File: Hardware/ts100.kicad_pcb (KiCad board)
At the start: 2 copper layers, 100 x 17 mm, 0 parts

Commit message: pcb
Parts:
- added C1: 0.1u, Capacitor_SMD:C_0603_1608Metric, F.Cu at (154.0, 137.6)
- added C10: 0.1u, Capacitor_SMD:C_0603_1608Metric, F.Cu at (148.9, 140.1)
- added C11: 0.1u, Capacitor_SMD:C_0603_1608Metric, F.Cu at (148.9, 142.6)
- added C12: 0.1u, Capacitor_SMD:C_0603_1608Metric, F.Cu at (153.0, 140.1)
- added C13: 0.1u, Capacitor_SMD:C_0603_1608Metric, F.Cu at (166.4, 128.7)
- added C2: 10u, Capacitor_SMD:C_0805_2012Metric, F.Cu at (161.1, 130.0)
- added C3: 0.1u, Capacitor_SMD:C_0603_1608Metric, F.Cu at (165.0, 140.0)
- added C4: 2.2n, Capacitor_SMD:C_0603_1608Metric, F.Cu at (173.3, 131.6)
- added C5: 10n, Capacitor_SMD:C_0603_1608Metric, F.Cu at (169.3, 131.2)
- added C6: 22u, Capacitor_SMD:C_0805_2012Metric, F.Cu at (156.2, 132.2)
- added C7: 22p, Capacitor_SMD:C_0603_1608Metric, F.Cu at (160.0, 135.0)
- added C8: 22p, Capacitor_SMD:C_0603_1608Metric, F.Cu at (156.0, 135.0)
- added C9: 0.1u, Capacitor_SMD:C_0603_1608Metric, F.Cu at (150.0, 137.6)
- added D1: 1N5819, Diode_SMD:D_SMA, F.Cu at (142.9, 140.4)
- added J2: Iron+, ts100:Fuseholder_5x20mm_inline, F.Cu at (137.2, 119.6)
- added J3: Iron-, ts100:Fuseholder_5x20mm_inline, F.Cu at (141.9, 103.8)
- added J4: GND, ts100:Fuseholder_5x20mm_inline, F.Cu at (99.3, 102.9)
- added J5: SWD, Connector_PinHeader_1.27mm:PinHeader_2x03_P1.27mm_Vertical, F.Cu at (161.0, 124.3)
- added L1: 6.8u, ts100:Inductor_SMD_5x4.5mm, F.Cu at (149.4, 133.5)
- added Q1: 2SC3356, Package_TO_SOT_SMD:SOT-23, F.Cu at (166.6, 125.1)
- added Q2: IRF4905STRLPBF, Package_TO_SOT_SMD:TO-263-2, B.Cu at (125.0, 101.1)
- added R1: 1k, Resistor_SMD:R_0603_1608Metric, F.Cu at (168.0, 133.7)
- added R10: 10k, Resistor_SMD:R_0603_1608Metric, F.Cu at (170.8, 124.1)
- added R11: 31.25k, Resistor_SMD:R_0603_1608Metric, F.Cu at (161.0, 140.0)
- added R12: 1M, Resistor_SMD:R_0603_1608Metric, F.Cu at (173.3, 129.1)
- added R13: 10k, Resistor_SMD:R_0603_1608Metric, F.Cu at (161.0, 142.5)
- added R14: 10k, Resistor_SMD:R_0603_1608Metric, F.Cu at (166.0, 136.2)
- added R2: 1k, Resistor_SMD:R_0603_1608Metric, F.Cu at (153.0, 142.6)
- added R3: 100k, Resistor_SMD:R_0603_1608Metric, F.Cu at (158.0, 137.5)
- added R4: 1k, Resistor_SMD:R_0603_1608Metric, F.Cu at (165.3, 131.2)
- added R5: 10k, Resistor_SMD:R_0603_1608Metric, F.Cu at (170.8, 126.6)
- added R6: 10k, Resistor_SMD:R_0603_1608Metric, F.Cu at (157.0, 140.1)
- added R7: 51k, Resistor_SMD:R_0603_1608Metric, F.Cu at (164.0, 133.7)
- added R8: 10k, Resistor_SMD:R_0603_1608Metric, F.Cu at (157.0, 142.6)
- added R9: 1k, Resistor_SMD:R_0603_1608Metric, F.Cu at (162.0, 137.5)
- added RV1: 500k, ts100:3362P, F.Cu at (170.2, 118.7)
- added U1: AD823, Package_SO:SOP-8_3.9x4.9mm_P1.27mm, F.Cu at (134.7, 141.4)
- added U2: EUP3476, Package_SO:SOIC-8-1EP_3.9x4.9mm_P1.27mm_EP2.29x3mm_ThermalVias, F.Cu at (126.2, 140.5)
- added U3: 1N4728A, Diode_THT:D_DO-41_SOD81_P7.62mm_Horizontal, F.Cu at (123.9, 135.2)
- added U4: 128x32 OLED, Connector_PinSocket_2.54mm:PinSocket_1x04_P2.54mm_Vertical, F.Cu at (156.5, 97.5)
- added U5: STM32F103C8T6, Package_QFP:LQFP-48_7x7mm_P0.5mm, F.Cu at (142.3, 132.5)
- added Y1: 8M, Crystal:Crystal_SMD_HC49-SD, F.Cu at (129.3, 129.9)

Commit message: pcb
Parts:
- added J1: Jack-DC, KIGIT_Connector:DC-050_2.5x5.5mm_SMT, F.Cu at (193.9, 106.4)
- added S1: SW18010P, Capacitor_THT:C_Radial_D5.0mm_H5.0mm_P2.00mm, B.Cu at (115.0, 100.0)
- added SW1: SW_Push, ts100:SMD,4.6x1.82x3.5mm, F.Cu at (115.5, 94.1)
- added SW2: SW_Push, ts100:SMD,4.6x1.82x3.5mm, F.Cu at (115.5, 108.0)
- C1, C10, C11, C12, C13, C7, C8, C9, D1, R10, R12, R13, R14, R4, R7, R9, RV1, U1, U3, U5, Y1: moved to B.Cu
- J5: footprint Connector_PinHeader_1.27mm:PinHeader_2x03_P1.27mm_Vertical -> Connector_PinHeader_1.27mm:PinHeader_1x06_P1.27mm_Vertical
- Q2: moved to F.Cu
- moved D1 75.9 mm to (142.5, 64.5)
- moved RV1 75.7 mm to (112.8, 69.3)
- moved C1 75.3 mm to (135.1, 64.7)
- moved R9 74.7 mm to (159.7, 62.9)
- moved R7 74.5 mm to (151.9, 60.1)
- moved U3 74.3 mm to (157.3, 68.8)
- moved U1 72.5 mm to (103.8, 75.8)
- moved U2 69.2 mm to (194.6, 151.2)
- moved R4 67.9 mm to (151.0, 64.8)
- moved R10 67.2 mm to (158.2, 58.1)
- moved J5 65.2 mm to (103.2, 94.2), turned to 270 degrees
- moved Q1 63.5 mm to (106.5, 145.5)
- moved R5 60.9 mm to (111.6, 140.8)
- moved C6 57.6 mm to (210.7, 151.0)
- moved R2 55.5 mm to (204.2, 163.9)
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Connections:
- J5 pad 1: +3V3 -> GND
- J5 pad 2: GND -> +3V3
- J5 pad 4: /SWDCLK -> /SWO
- J5 pad 5: /SWO -> /SWDCLK
- U5 pad 21: Net-(U5-Pad21) -> /WAK_UP
- U5 pad 45: Net-(U5-Pad45) -> /KEY1
- U5 pad 46: Net-(U5-Pad46) -> /KEY2

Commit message: 修改封装
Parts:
- removed R14: 10k, Resistor_SMD:R_0603_1608Metric
- removed SW1, SW2: SW_Push, ts100:SMD,4.6x1.82x3.5mm
- added C14: 0.1u, Capacitor_SMD:C_0402_1005Metric, F.Cu at (191.0, 80.0)
- added D2: 1N5819, Diode_SMD:D_SOD-123, F.Cu at (182.8, 75.3)
- added FB1: 600@100MHz, Inductor_SMD:L_0805_2012Metric, F.Cu at (187.3, 78.9)
- added K1: TMP_UP, ts100:SMD,4.6x1.82x3.5mm, F.Cu at (181.9, 79.3)
- added K2: TMP_DOWN, ts100:SMD,4.6x1.82x3.5mm, F.Cu at (189.9, 74.7)
- added L2: 39n, Inductor_SMD:L_0402_1005Metric, F.Cu at (191.0, 78.0)
- C1: value 0.1u -> 10u 50V; footprint Capacitor_SMD:C_0603_1608Metric -> Capacitor_SMD:C_1210_3225Metric
- C10: value 0.1u -> 1u; footprint Capacitor_SMD:C_0603_1608Metric -> Capacitor_SMD:C_0402_1005Metric
- C11: value 0.1u -> 10n; footprint Capacitor_SMD:C_0603_1608Metric -> Capacitor_SMD:C_0402_1005Metric
- C12, C13: value 0.1u -> 12p; footprint Capacitor_SMD:C_0603_1608Metric -> Capacitor_SMD:C_0402_1005Metric
- C2: value 10u -> 10n; footprint Capacitor_SMD:C_0805_2012Metric -> Capacitor_SMD:C_0603_1608Metric
- C3: value 0.1u -> 22u 6.3V
- C4: value 2.2n -> 0.1u
- C5: value 10n -> 4u7; footprint Capacitor_SMD:C_0603_1608Metric -> Capacitor_SMD:C_0402_1005Metric
- C6: value 22u -> 0.1u; footprint Capacitor_SMD:C_0805_2012Metric -> Capacitor_SMD:C_0402_1005Metric
- C7, C8: value 22p -> 0.1u; footprint Capacitor_SMD:C_0603_1608Metric -> Capacitor_SMD:C_0402_1005Metric
- C9: footprint Capacitor_SMD:C_0603_1608Metric -> Capacitor_SMD:C_0402_1005Metric
- D1: value 1N5819 -> B5819W; footprint Diode_SMD:D_SMA -> Diode_SMD:D_SOD-123
- J2: value Iron+ -> SWD; footprint ts100:Fuseholder_5x20mm_inline -> Connector_PinHeader_1.27mm:PinHeader_1x06_P1.27mm_Vertical
- J3: value Iron- -> Iron+
- J4: value GND -> Iron-
- J5: value SWD -> GND; footprint Connector_PinHeader_1.27mm:PinHeader_1x06_P1.27mm_Vertical -> ts100:Fuseholder_5x20mm_inline
- L1: value 6.8u -> 4.7u; footprint ts100:Inductor_SMD_5x4.5mm -> Inductor_SMD:L_1008_2520Metric
- R1: value 1k -> 75k
- R10: value 10k -> 1k; footprint Resistor_SMD:R_0603_1608Metric -> Resistor_SMD:R_0402_1005Metric
- R11: value 31.25k -> 51k; footprint Resistor_SMD:R_0603_1608Metric -> Resistor_SMD:R_0402_1005Metric
- R12: value 1M -> 1k; footprint Resistor_SMD:R_0603_1608Metric -> Resistor_SMD:R_0402_1005Metric
- R13, R8, R9: footprint Resistor_SMD:R_0603_1608Metric -> Resistor_SMD:R_0402_1005Metric
- R2: value 1k -> 24k
- R3: value 100k -> DNP; footprint Resistor_SMD:R_0603_1608Metric -> Resistor_SMD:R_0402_1005Metric
- R4: value 1k -> 10k; footprint Resistor_SMD:R_0603_1608Metric -> Resistor_SMD:R_0402_1005Metric
- R5: value 10k -> 0R; footprint Resistor_SMD:R_0603_1608Metric -> Resistor_SMD:R_0402_1005Metric
- R6: value 10k -> 47 or DNP; footprint Resistor_SMD:R_0603_1608Metric -> Resistor_SMD:R_0402_1005Metric
- R7: value 51k -> 1k; footprint Resistor_SMD:R_0603_1608Metric -> Resistor_SMD:R_0402_1005Metric
- U1: value AD823 -> STM32F103C8T6; footprint Package_SO:SOP-8_3.9x4.9mm_P1.27mm -> Package_QFP:LQFP-48_7x7mm_P0.5mm
- U2: value EUP3476 -> 128x32 OLED; footprint Package_SO:SOIC-8-1EP_3.9x4.9mm_P1.27mm_EP2.29x3mm_ThermalVias -> Connector_PinSocket_2.54mm:PinSocket_1x04_P2.54mm_Vertical
- U3: value 1N4728A -> AD823; footprint Diode_THT:D_DO-41_SOD81_P7.62mm_Horizontal -> Package_SO:SOP-8_3.9x4.9mm_P1.27mm
- U4: value 128x32 OLED -> MP2359DJ-LF-Z; footprint Connector_PinSocket_2.54mm:PinSocket_1x04_P2.54mm_Vertical -> Package_TO_SOT_SMD:SOT-23-6
- U5: value STM32F103C8T6 -> 1N4728A; footprint Package_QFP:LQFP-48_7x7mm_P0.5mm -> Diode_SMD:D_SOD-123
- Y1: value 8M -> 16M; footprint Crystal:Crystal_SMD_HC49-SD -> Crystal:Crystal_SMD_3225-4Pin_3.2x2.5mm
- moved J2 42.4 mm to (109.3, 94.4)
- moved J5 24.2 mm to (112.1, 116.7)
- moved U5 15.5 mm to (161.4, 85.9)
- moved RV1 3.95 mm to (116.8, 69.0)
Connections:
- C1 pad 1: GND -> +15V
- C1 pad 2: +3V3 -> GND
- C10 pad 1: GND -> +3.3VA
- C10 pad 2: +3V3 -> GND
- C11 pad 1: GND -> +3.3VA
- C11 pad 2: +3V3 -> GND
- C12 pad 1: GND -> /HSE_IN
- C12 pad 2: +3V3 -> GND
- C13 pad 1: GND -> Net-(C13-Pad1)
- C13 pad 2: +3V3 -> GND
- C2 pad 1: +15V -> Net-(C2-Pad1)
- C2 pad 2: GND -> Net-(C2-Pad2)
- C3 pad 1: Net-(C3-Pad1) -> +3V3
- C4 pad 2: Net-(C4-Pad2) -> /NRST
- C5 pad 1: Net-(C5-Pad1) -> +3V3
- C5 pad 2: Net-(C5-Pad2) -> GND
- C6 pad 1: GND -> +3V3
- C6 pad 2: +3V3 -> GND
- C7 pad 1: Net-(C7-Pad1) -> +3V3
- C8 pad 1: Net-(C8-Pad1) -> +3V3
- C9 pad 1: GND -> +3V3
- C9 pad 2: /NRST -> GND
- D1 pad 1: Net-(D1-Pad1) -> Net-(C2-Pad1)
- D1 pad 2: /TEMP_ADC -> GND
- J2 pad 1: /Iron+ -> GND
- J3 pad 1: GND -> /Iron+
- L1 pad 1: Net-(C5-Pad1) -> Net-(C2-Pad1)
- R1 pad 1: Net-(Q1-Pad1) -> Net-(R1-Pad1)
- R1 pad 2: /PWM -> +3V3
- R10 pad 1: /Iron+ -> Net-(R10-Pad1)
- R10 pad 2: Net-(R10-Pad2) -> /TEMP_ADC
- R11 pad 1: +3V3 -> Net-(R11-Pad1)
- R12 pad 1: Net-(C8-Pad1) -> GND
- R12 pad 2: Net-(C7-Pad1) -> Net-(R11-Pad1)
- R13 pad 1: Net-(R13-Pad1) -> /Iron+
- R13 pad 2: GND -> Net-(R13-Pad2)
- R2 pad 1: +3V3 -> GND
- R2 pad 2: Net-(D1-Pad1) -> Net-(R1-Pad1)
- R3 pad 1: +15V -> Net-(R3-Pad1)
- R3 pad 2: Net-(R3-Pad2) -> +3V3
- R4 pad 1: Net-(R4-Pad1) -> /BOOT0
- R4 pad 2: /TEMP_ADC -> Net-(R3-Pad1)
- R5 pad 1: +15V -> GND
- R5 pad 2: Net-(Q1-Pad3) -> Net-(R3-Pad1)
- R6 pad 1: Net-(R6-Pad1) -> Net-(C13-Pad1)
- R6 pad 2: Net-(C4-Pad2) -> /HSE_OUT
- R7 pad 1: Net-(R7-Pad1) -> Net-(Q1-Pad1)
- R7 pad 2: Net-(R7-Pad2) -> /PWM
- R8 pad 1: GND -> +15V
- R8 pad 2: Net-(R11-Pad2) -> Net-(Q1-Pad3)
- R9 pad 1: GND -> +3V3
- R9 pad 2: Net-(R7-Pad1) -> Net-(D2-Pad1)
- RV1 pad 1: Net-(R4-Pad1) -> Net-(R10-Pad1)
- RV1 pad 2: Net-(R4-Pad1) -> Net-(R10-Pad1)
- RV1 pad 3: Net-(R7-Pad2) -> Net-(R11-Pad2)
- U1 pad 1: Net-(R4-Pad1) -> +3V3
- U1 pad 2: Net-(R7-Pad1) -> (no net)
- U1 pad 3: Net-(R10-Pad2) -> (no net)
- U1 pad 4: GND -> (no net)
- U1 pad 5: Net-(U1-Pad5) -> /HSE_IN
- U1 pad 6: Net-(U1-Pad6) -> /HSE_OUT
- U1 pad 7: Net-(U1-Pad7) -> /NRST
- U1 pad 8: +3V3 -> GND
- U2 pad 1: Net-(C5-Pad2) -> GND
- U2 pad 2: +15V -> +3V3
- U2 pad 3: Net-(C5-Pad1) -> /SCL
- U2 pad 4: GND -> /SDA
- U3 pad 1: Net-(R10-Pad2) -> Net-(R10-Pad1)
- U3 pad 2: GND -> Net-(R11-Pad1)
- U4 pad 1: GND -> Net-(C2-Pad2)
- U4 pad 2: +3V3 -> GND
- U4 pad 3: /SCL -> Net-(R1-Pad1)
- U4 pad 4: /SDA -> +15V
- U5 pad 1: +3V3 -> Net-(R13-Pad2)
- U5 pad 2: Net-(U5-Pad2) -> GND
- Y1 pad 1: Net-(C7-Pad1) -> /HSE_IN
- Y1 pad 2: Net-(C8-Pad1) -> GND
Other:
- copper layers 2 -> 4

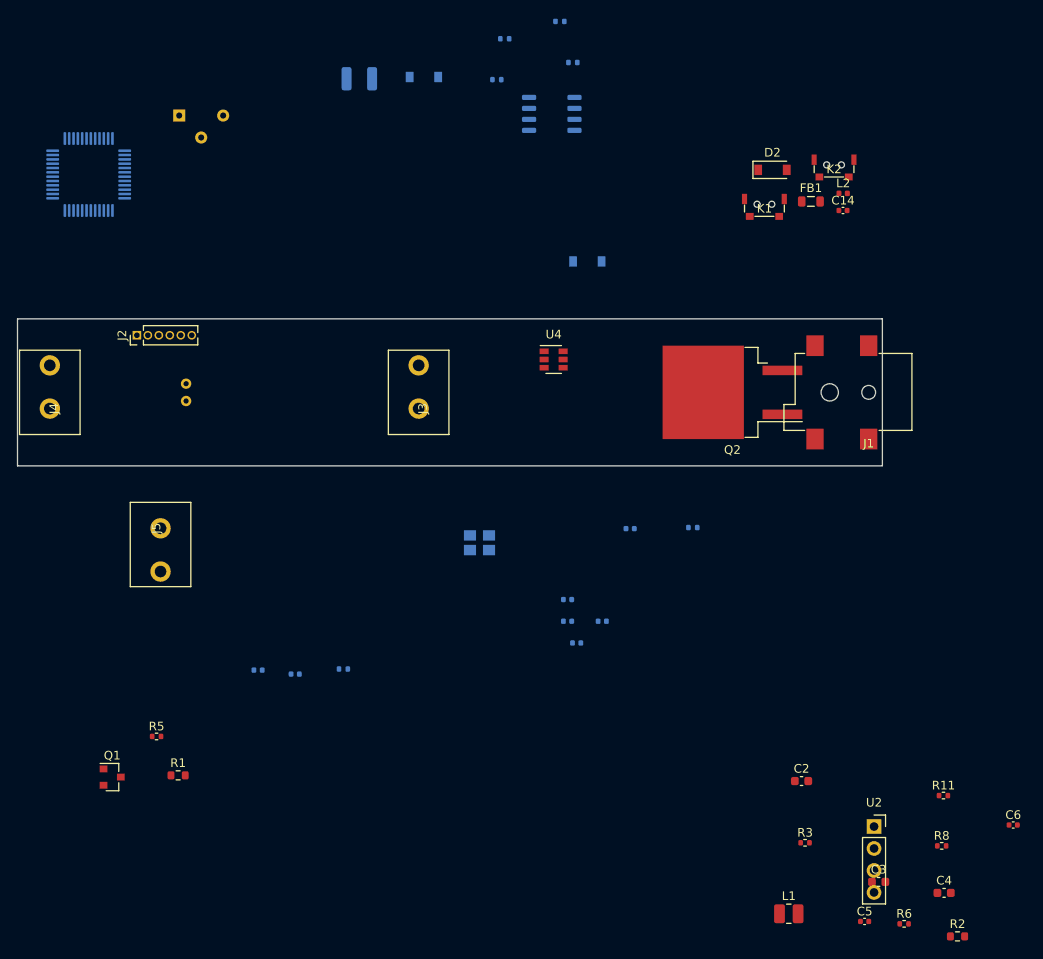
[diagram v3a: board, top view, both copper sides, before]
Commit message: 重绘PCB
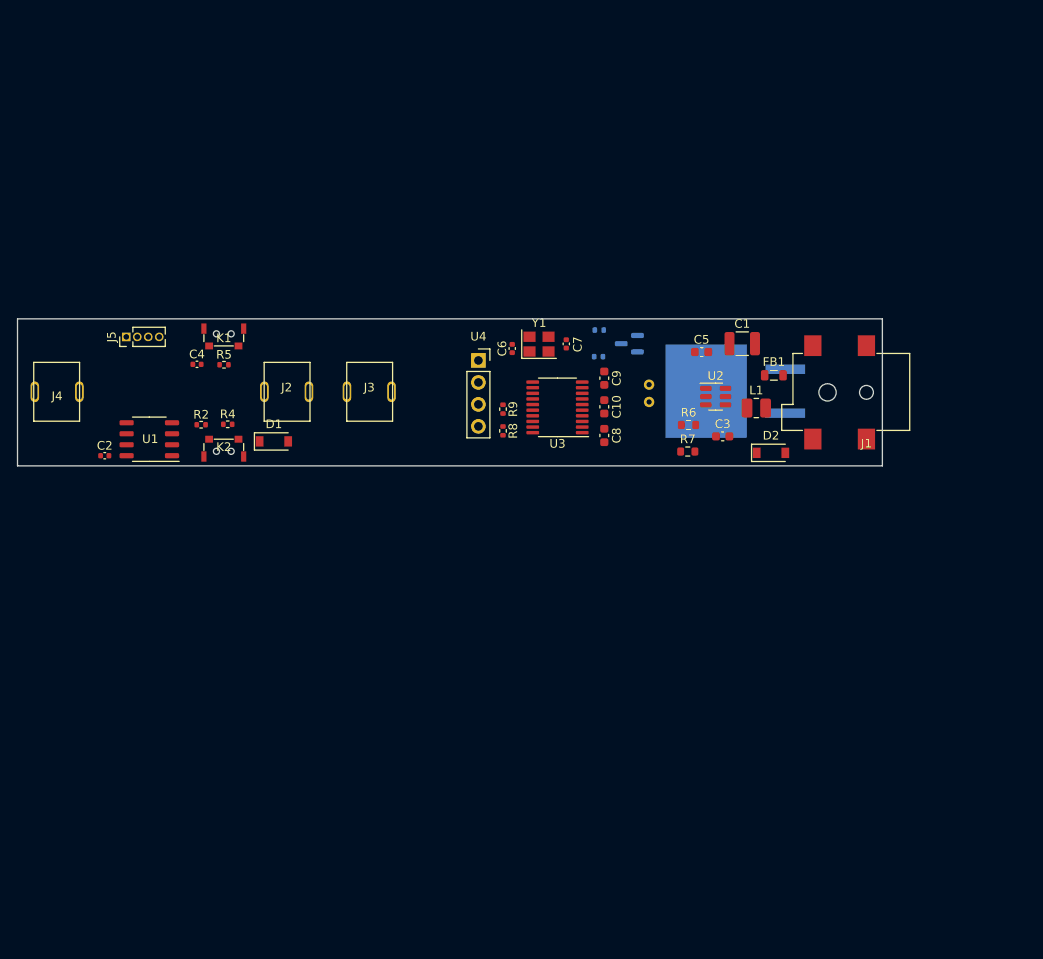
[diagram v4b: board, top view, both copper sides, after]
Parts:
- removed C11: 10n, Capacitor_SMD:C_0402_1005Metric
- removed C12, C13: 12p, Capacitor_SMD:C_0402_1005Metric
- removed C14: 0.1u, Capacitor_SMD:C_0402_1005Metric
- removed the J2 at (109.3, 94.4)
- removed L2: 39n, Inductor_SMD:L_0402_1005Metric
- removed R10, R12: 1k, Resistor_SMD:R_0402_1005Metric
- removed R11: 51k, Resistor_SMD:R_0402_1005Metric
- removed R13: 10k, Resistor_SMD:R_0402_1005Metric
- removed RV1: 500k, ts100:3362P
- removed U5: 1N4728A, Diode_SMD:D_SOD-123
- added J5: Debug, Connector_PinHeader_1.27mm:PinHeader_1x04_P1.27mm_Vertical, F.Cu at (108.1, 94.6)
- C1, Y1: moved to F.Cu
- C10: value 1u -> 0.1u; footprint Capacitor_SMD:C_0402_1005Metric -> Capacitor_SMD:C_0603_1608Metric; moved to F.Cu
- C2: value 10n -> 0.1u; footprint Capacitor_SMD:C_0603_1608Metric -> Capacitor_SMD:C_0402_1005Metric
- C3: value 22u 6.3V -> 10n
- C4: value 0.1u -> 2.2n; footprint Capacitor_SMD:C_0603_1608Metric -> Capacitor_SMD:C_0402_1005Metric
- C5: value 4u7 -> 22u 6.3V; footprint Capacitor_SMD:C_0402_1005Metric -> Capacitor_SMD:C_0603_1608Metric
- C6: value 0.1u -> 12p
- C7: value 0.1u -> 12p; moved to F.Cu
- C8: footprint Capacitor_SMD:C_0402_1005Metric -> Capacitor_SMD:C_0603_1608Metric; moved to F.Cu
- C9: value 0.1u -> 1u; footprint Capacitor_SMD:C_0402_1005Metric -> Capacitor_SMD:C_0603_1608Metric; moved to F.Cu
- D1: value B5819W -> 1N5819; moved to F.Cu
- D2: value 1N5819 -> B5819W
- J1: footprint KIGIT_Connector:DC-050_2.5x5.5mm_SMT -> KIGIT_Connectors:DC-050_2.5x5.5mm_SMT
- L1: value 4.7u -> 6.8u
- Q1, Q2: moved to B.Cu
- R1: value 75k -> 1k; footprint Resistor_SMD:R_0603_1608Metric -> Resistor_SMD:R_0402_1005Metric; moved to B.Cu
- R2: value 24k -> 200k; footprint Resistor_SMD:R_0603_1608Metric -> Resistor_SMD:R_0402_1005Metric
- R3: value DNP -> 10k; moved to B.Cu
- R4: value 10k -> 1k; moved to F.Cu
- R5: value 0R -> 10k
- R6: value 47 or DNP -> 68k 1%; footprint Resistor_SMD:R_0402_1005Metric -> Resistor_SMD:R_0603_1608Metric
- R7: value 1k -> 13k 1%; footprint Resistor_SMD:R_0402_1005Metric -> Resistor_SMD:R_0603_1608Metric; moved to F.Cu
- R8: value 10k -> 4k7
- R9: value 1k -> 4k7; moved to F.Cu
- U1: value STM32F103C8T6 -> LM358G-S08-R; footprint Package_QFP:LQFP-48_7x7mm_P0.5mm -> Package_SO:SOP-8_3.9x4.9mm_P1.27mm; moved to F.Cu
- U2: value 128x32 OLED -> MP2359DJ-LF-Z; footprint Connector_PinSocket_2.54mm:PinSocket_1x04_P2.54mm_Vertical -> Package_TO_SOT_SMD:SOT-23-6
- U3: value AD823 -> STM8S103F3; footprint Package_SO:SOP-8_3.9x4.9mm_P1.27mm -> Package_SO:TSSOP-20_4.4x6.5mm_P0.65mm; moved to F.Cu
- U4: value MP2359DJ-LF-Z -> 128x32 OLED; footprint Package_TO_SOT_SMD:SOT-23-6 -> Connector_PinSocket_2.54mm:PinSocket_1x04_P2.54mm_Vertical
- moved C4 105.8 mm to (116.3, 97.8)
- moved R2 105.6 mm to (116.8, 104.7)
- moved C2 88.9 mm to (105.6, 108.3)
- moved C6 79.9 mm to (152.7, 95.9), turned to 90 degrees
- moved Q1 78.0 mm to (166.3, 95.4), turned to 180 degrees
- moved K2 77.9 mm to (119.4, 107.8), turned to 180 degrees
- moved R1 70.9 mm to (162.8, 93.8), turned to 180 degrees
- moved R8 69.8 mm to (151.7, 105.5), turned to -90 degrees
- moved C5 68.5 mm to (174.6, 96.3)
- moved K1 64.3 mm to (119.4, 94.2)
- moved R6 62.8 mm to (173.1, 104.8)
- moved R3 61.1 mm to (162.7, 96.9), turned to 180 degrees
- moved L1 58.6 mm to (180.9, 102.8)
- moved C3 54.6 mm to (177.1, 106.1)
- moved C1 53.8 mm to (179.3, 95.4)
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- renumbered J3 to J2, J4 to J3, J5 to J4
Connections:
- C10 pad 1: +3.3VA -> GND
- C10 pad 2: GND -> +5V
- C2 pad 1: Net-(C2-Pad1) -> GND
- C2 pad 2: Net-(C2-Pad2) -> +5V
- C3 pad 1: +3V3 -> Net-(C3-Pad1)
- C3 pad 2: GND -> Net-(C3-Pad2)
- C4 pad 2: /NRST -> Net-(C4-Pad2)
- C5 pad 1: +3V3 -> +5V
- C6 pad 1: +3V3 -> /HSE_IN
- C7 pad 1: +3V3 -> /HSE_OUT
- C8 pad 1: +3V3 -> GND
- C8 pad 2: GND -> /NRST
- C9 pad 1: +3V3 -> Net-(C9-Pad1)
- D1 pad 1: Net-(C2-Pad1) -> Net-(C4-Pad2)
- D2 pad 1: Net-(D2-Pad1) -> Net-(C3-Pad1)
- D2 pad 2: /TEMP_ADC -> GND
- FB1 pad 1: (no net) -> +15V
- FB1 pad 2: +15V -> Net-(FB1-Pad2)
- J1 pad 1: +15V -> Net-(FB1-Pad2)
- L1 pad 1: Net-(C2-Pad1) -> Net-(C3-Pad1)
- L1 pad 2: +3V3 -> +5V
- R1 pad 1: Net-(R1-Pad1) -> Net-(Q1-Pad1)
- R1 pad 2: +3V3 -> /PWM
- R2 pad 1: GND -> Net-(R2-Pad1)
- R2 pad 2: Net-(R1-Pad1) -> /TEMP_ADC
- R3 pad 1: Net-(R3-Pad1) -> +15V
- R3 pad 2: +3V3 -> Net-(Q1-Pad3)
- R4 pad 1: /BOOT0 -> GND
- R4 pad 2: Net-(R3-Pad1) -> Net-(R2-Pad1)
- R5 pad 1: GND -> /Iron+
- R5 pad 2: Net-(R3-Pad1) -> Net-(C4-Pad2)
- R6 pad 1: Net-(C13-Pad1) -> Net-(R6-Pad1)
- R6 pad 2: /HSE_OUT -> +5V
- R7 pad 1: Net-(Q1-Pad1) -> GND
- R7 pad 2: /PWM -> Net-(R6-Pad1)
- R8 pad 1: +15V -> /SDA
- R8 pad 2: Net-(Q1-Pad3) -> +5V
- R9 pad 1: +3V3 -> /SCL
- R9 pad 2: Net-(D2-Pad1) -> +5V
- U1 pad 1: +3V3 -> /TEMP_ADC
- U1 pad 2: (no net) -> Net-(R2-Pad1)
- U1 pad 3: (no net) -> Net-(C4-Pad2)
- U1 pad 4: (no net) -> GND
- U1 pad 5: /HSE_IN -> unconnected-(U1-Pad5)
- U1 pad 6: /HSE_OUT -> unconnected-(U1-Pad6)
- U1 pad 7: /NRST -> unconnected-(U1-Pad7)
- U1 pad 8: GND -> +5V
- U2 pad 1: GND -> Net-(C3-Pad2)
- U2 pad 2: +3V3 -> GND
- U2 pad 3: /SCL -> Net-(R6-Pad1)
- U2 pad 4: /SDA -> +15V
- U3 pad 1: Net-(R10-Pad1) -> /KEY1
- U3 pad 2: Net-(R11-Pad1) -> /KEY2
- U3 pad 3: Net-(R13-Pad2) -> /WAK_UP
- U3 pad 4: GND -> /NRST
- U3 pad 5: (no net) -> /HSE_IN
- U3 pad 6: (no net) -> /HSE_OUT
- U3 pad 7: (no net) -> GND
- U3 pad 8: +3V3 -> Net-(C9-Pad1)
- U4 pad 1: Net-(C2-Pad2) -> GND
- U4 pad 2: GND -> +5V
- U4 pad 3: Net-(R1-Pad1) -> /SCL
- U4 pad 4: +15V -> /SDA
- Y1 pad 3: Net-(C13-Pad1) -> /HSE_OUT
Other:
- copper layers 4 -> 2
- net class Default removed

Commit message: 修改封装
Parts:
- C8: footprint Capacitor_SMD:C_0603_1608Metric -> Capacitor_SMD:C_0402_1005Metric
- J1: footprint KIGIT_Connectors:DC-050_2.5x5.5mm_SMT -> Connector_BarrelJack:BarrelJack_CLIFF_FC681465S_SMT_Horizontal
- R6, R7: footprint Resistor_SMD:R_0603_1608Metric -> Resistor_SMD:R_0402_1005Metric
- moved J1 6.11 mm to (190.8, 101.0), turned to 180 degrees
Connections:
- U3 pad 18: unconnected-(U3-Pad18) -> /SWIM
